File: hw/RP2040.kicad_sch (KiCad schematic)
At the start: 31 parts, among them SW2 SW_DIP_x04, U5 W25Q128JVSIQ, U6 RP2040, Y1 Crystal_GND24

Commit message: hw: WIP
Signed-off-by: Mahyar Koshkouei <mk@deltabeard.com>
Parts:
- C11, C12: footprint Capacitor_SMD:C_0603_1608Metric -> Capacitor_SMD:C_0402_1005Metric; LCSC C22397 -> C1570; MFr CL10C300JB8NNNC -> 0402CG300J500NT; Manufacturer Samsung Electro-Mechanics -> FH(Guangdong Fenghua Advanced Tech)
- C15, C22, C9: footprint Capacitor_SMD:C_0603_1608Metric -> Capacitor_SMD:C_0402_1005Metric; LCSC C15849 -> C52923; MFr CL10A105KB8NNNC -> CL05A105KA5NQNC; Manufacturer Samsung Electro-Mechanics -> Samsung Electro-Mechanics
- R6: renamed from R7; Manufacturer UNI-ROYAL(Uniroyal Elec) -> UNI-ROYAL(Uniroyal Elec)
- R7: renamed from R8; Manufacturer UNI-ROYAL(Uniroyal Elec) -> UNI-ROYAL(Uniroyal Elec)
- R8: renamed from R9; Manufacturer UNI-ROYAL(Uniroyal Elec) -> UNI-ROYAL(Uniroyal Elec)
- TP10: renamed from TP15; value TestPoint_Small -> TestPoint
- TP11: renamed from TP16; value TestPoint_Small -> TestPoint
- TP3: renamed from TP8; footprint TestPoint:TestPoint_Pad_D1.0mm -> TestPoint:TestPoint_THTPad_D1.0mm_Drill0.5mm
- TP4: renamed from TP9; footprint TestPoint:TestPoint_Pad_D1.0mm -> TestPoint:TestPoint_THTPad_D1.0mm_Drill0.5mm
- TP5: renamed from TP10; value SWCLK -> TestPoint; footprint TestPoint:TestPoint_Pad_D1.0mm -> TestPoint:TestPoint_THTPad_D1.0mm_Drill0.5mm
- TP6: renamed from TP11; value SWDIO -> TestPoint; footprint TestPoint:TestPoint_Pad_D1.0mm -> TestPoint:TestPoint_THTPad_D1.0mm_Drill0.5mm
- TP7: renamed from TP12; value GND -> TestPoint; footprint TestPoint:TestPoint_Pad_D1.0mm -> TestPoint:TestPoint_THTPad_D1.0mm_Drill0.5mm
- TP8: renamed from TP13; value TestPoint_Small -> TestPoint
- TP9: renamed from TP14; value TestPoint_Small -> TestPoint
- renumbered R10 to R9, SW2 to SW1
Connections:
- net I2C_{SCLK}: now also U6.12 (GPIO9); no longer U6.14 (GPIO11)
- net I2C_{SDA}: now also U6.11 (GPIO8); no longer U6.13 (GPIO10)
- net SPI0_{MOSI}: now also U6.5 (GPIO3); no longer U6.9 (GPIO7)
- net SWITCH: now also U6.13 (GPIO10); no longer U6.12 (GPIO9)
- new net MOTOR: U6.14 (GPIO11)
- no-connect marks 3 -> 2
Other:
- moved on the sheet: SW1

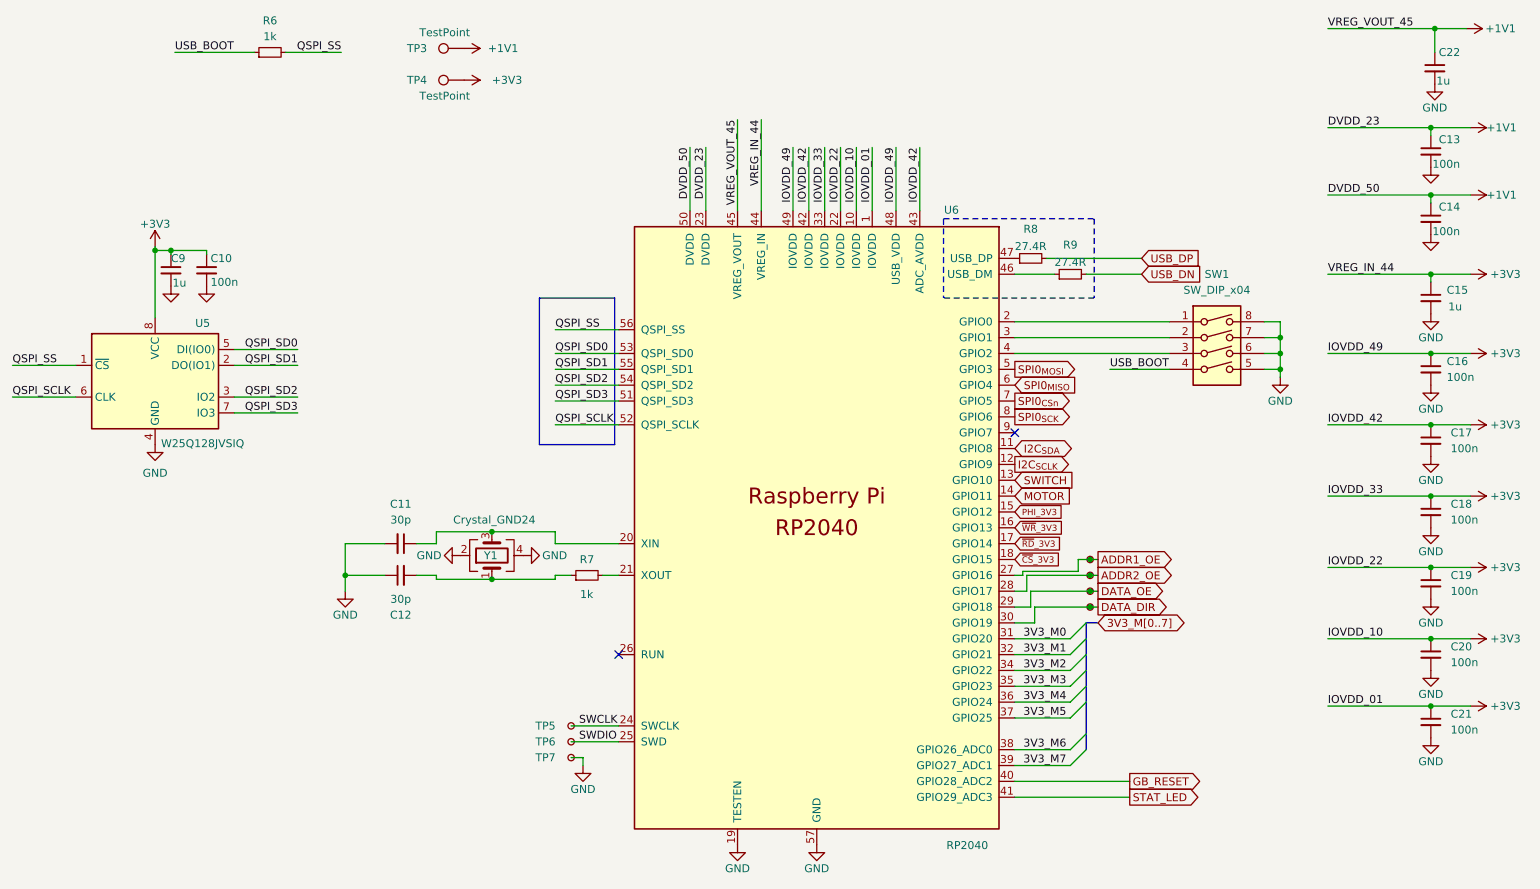
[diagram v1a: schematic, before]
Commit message: hw: remove DIP switch and LED
Signed-off-by: Mahyar Koshkouei <mk@deltabeard.com>
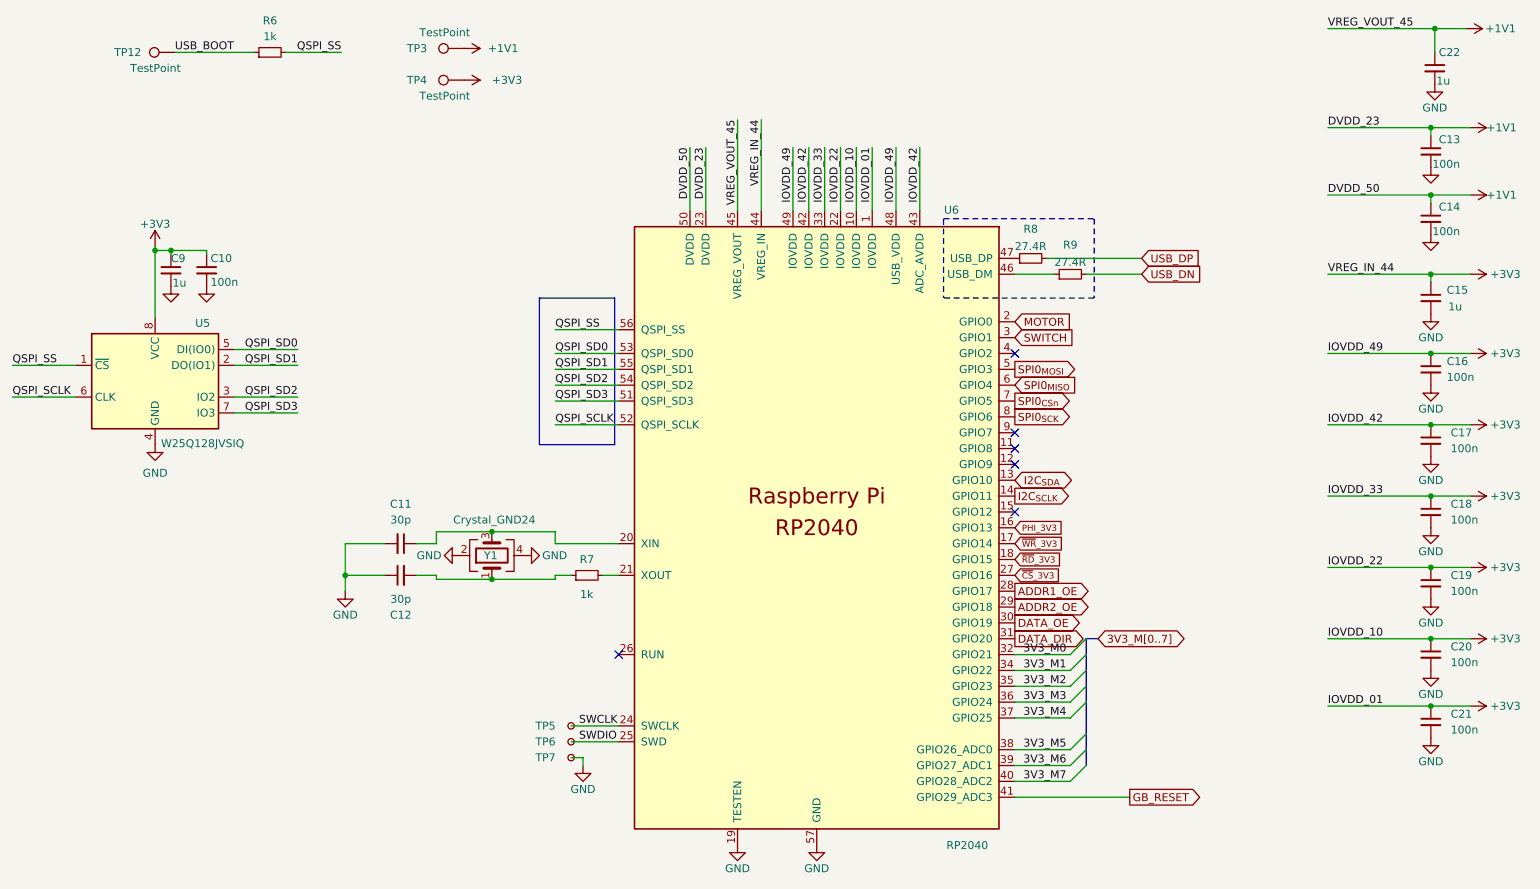
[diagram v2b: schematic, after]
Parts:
- removed SW1: SW_DIP_x04, Button_Switch_SMD:SW_DIP_SPSTx04_Slide_6.7x11.72mm_W8.61mm_P2.54mm_LowProfile, symbol Switch:SW_DIP_x04
- removed TP10, TP11, TP8, TP9: TestPoint, TestPoint:TestPoint_Pad_D1.0mm, symbol Connector:TestPoint_Small
- added TP12: TestPoint, TestPoint:TestPoint_THTPad_D1.0mm_Drill0.5mm, symbol Connector:TestPoint
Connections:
- net STAT_LED is gone; now on net GB_RESET: U6.41 (GPIO29_ADC3)
- net 3V3_M0: now also U6.32 (GPIO21); no longer U6.31 (GPIO20)
- net 3V3_M1: now also U6.34 (GPIO22); no longer U6.32 (GPIO21)
- net 3V3_M2: now also U6.35 (GPIO23); no longer U6.34 (GPIO22)
- net 3V3_M3: now also U6.36 (GPIO24); no longer U6.35 (GPIO23)
- net 3V3_M4: now also U6.37 (GPIO25); no longer U6.36 (GPIO24)
- net 3V3_M5: now also U6.38 (GPIO26_ADC0); no longer U6.37 (GPIO25)
- net 3V3_M6: now also U6.39 (GPIO27_ADC1); no longer U6.38 (GPIO26_ADC0)
- net 3V3_M7: now also U6.40 (GPIO28_ADC2); no longer U6.39 (GPIO27_ADC1)
- net ADDR1_OE: now also U6.28 (GPIO17); no longer U6.27 (GPIO16)
- net ADDR2_OE: now also U6.29 (GPIO18); no longer U6.28 (GPIO17)
- net DATA_DIR: now also U6.31 (GPIO20); no longer U6.30 (GPIO19)
- net DATA_OE: now also U6.30 (GPIO19); no longer U6.29 (GPIO18)
- net GB_RESET: no longer U6.40 (GPIO28_ADC2)
- net I2C_{SCLK}: now also U6.14 (GPIO11); no longer U6.12 (GPIO9)
- net I2C_{SDA}: now also U6.13 (GPIO10); no longer U6.11 (GPIO8)
- net MOTOR: now also U6.2 (GPIO0); no longer U6.14 (GPIO11)
- net PHI_3V3: now also U6.16 (GPIO13); no longer U6.15 (GPIO12)
- net SWITCH: now also U6.3 (GPIO1); no longer U6.13 (GPIO10)
- net USB_BOOT: now also TP12.1
- net ~{CS}_3V3: now also U6.27 (GPIO16); no longer U6.18 (GPIO15)
- net ~{RD}_3V3: now also U6.18 (GPIO15); no longer U6.17 (GPIO14)
- net ~{WR}_3V3: now also U6.17 (GPIO14); no longer U6.16 (GPIO13)
- no-connect marks 2 -> 6
